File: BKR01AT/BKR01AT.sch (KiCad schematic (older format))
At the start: 44 parts, among them J1 Conn_02x03_Odd_Even, SW1 SW_Push, SW2 SW_Push, SW3 SW_Push, U1 LIS2DHTR, Y1 32MHz, Y2 32.768kHz

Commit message: WIP: PCB
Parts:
- AE1: footprint antena_ble:2450AT18B100 -> 2450AT18B100E:ANT_2450AT18B100E
- D1, D2, D3: footprint (none) -> LED_SMD:LED_0603_1608Metric
- FID1, FID2: footprint (none) -> Fiducial:Fiducial_0.5mm_Mask1mm
- MCU1: footprint (none) -> Package_DFN_QFN:QFN-48-1EP_6x6mm_P0.4mm_EP4.6x4.6mm
- SW1, SW2, SW3: footprint (none) -> Button_Switch_THT:SW_PUSH_6mm_H4.3mm
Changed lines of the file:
@@
 F 0 "SW1" H 9650 5530 50  0000 C CNN
 F 1 "SW_Push" H 9650 5439 50  0000 C CNN
-F 2 "" H 9650 5445 50  0001 C CNN
+F 2 "Button_Switch_THT:SW_PUSH_6mm_H4.3mm" H 9650 5445 50  0001 C CNN
 F 3 "~" H 9650 5445 50  0001 C CNN
 F 4 "PTS636 SL43 LFS" H 9650 5245 50  0001 C CNN "Part Number"
@@
 F 0 "SW3" H 8880 5550 50  0000 C CNN
 F 1 "SW_Push" H 8880 5459 50  0000 C CNN
-F 2 "" H 8880 5465 50  0001 C CNN
+F 2 "Button_Switch_THT:SW_PUSH_6mm_H4.3mm" H 8880 5465 50  0001 C CNN
 F 3 "~" H 8880 5465 50  0001 C CNN
 F 4 "PTS636 SL43 LFS" H 8880 5265 50  0001 C CNN "Part Number"
@@
 F 0 "SW2" H 8055 5535 50  0000 C CNN
 F 1 "SW_Push" H 8055 5444 50  0000 C CNN
-F 2 "" H 8055 5450 50  0001 C CNN
+F 2 "Button_Switch_THT:SW_PUSH_6mm_H4.3mm" H 8055 5450 50  0001 C CNN
 F 3 "~" H 8055 5450 50  0001 C CNN
 F 4 "PTS636 SL43 LFS" H 8055 5250 50  0001 C CNN "Part Number"
@@
 F 0 "D2" V 8752 3313 50  0000 L CNN
 F 1 "Red LED" V 8843 3313 50  0000 L CNN
-F 2 "" H 8805 3235 50  0001 C CNN
+F 2 "LED_SMD:LED_0603_1608Metric" H 8805 3235 50  0001 C CNN
 F 3 "~" H 8805 3235 50  0001 C CNN
 F 4 "150060VS75000" H 8805 3235 50  0001 C CNN "Part Number"
@@
 F 0 "D3" V 8012 3338 50  0000 L CNN
 F 1 "Red LED" V 8103 3338 50  0000 L CNN
-F 2 "" H 8065 3260 50  0001 C CNN
+F 2 "LED_SMD:LED_0603_1608Metric" H 8065 3260 50  0001 C CNN
 F 3 "~" H 8065 3260 50  0001 C CNN
 F 4 "150060RS75000" H 8065 3260 50  0001 C CNN "Part Number"
@@
 F 0 "D1" V 9562 3298 50  0000 L CNN
 F 1 "Green LED" V 9653 3298 50  0000 L CNN
-F 2 "" H 9615 3220 50  0001 C CNN
+F 2 "LED_SMD:LED_0603_1608Metric" H 9615 3220 50  0001 C CNN
 F 3 "~" H 9615 3220 50  0001 C CNN
 F 4 "150060VS75000" H 9615 3220 50  0001 C CNN "Part Number"
@@
 F 0 "FID2" H 7430 6176 50  0000 L CNN
 F 1 "Fiducial" H 7430 6085 50  0000 L CNN
-F 2 "" H 7345 6130 50  0001 C CNN
+F 2 "Fiducial:Fiducial_0.5mm_Mask1mm" H 7345 6130 50  0001 C CNN
 F 3 "~" H 7345 6130 50  0001 C CNN
 	1    7345 6130
@@
 F 0 "FID1" H 8095 6151 50  0000 L CNN
 F 1 "Fiducial" H 8095 6060 50  0000 L CNN
-F 2 "" H 8010 6105 50  0001 C CNN
+F 2 "Fiducial:Fiducial_0.5mm_Mask1mm" H 8010 6105 50  0001 C CNN
 F 3 "~" H 8010 6105 50  0001 C CNN
 	1    8010 6105
@@
 F 0 "MCU1" H 3600 3390 50  0000 L CNN
 F 1 "nRF52832-QFAB-R" H 3335 3305 50  0000 L CNN
-F 2 "" H 3705 3330 50  0001 C CNN
+F 2 "Package_DFN_QFN:QFN-48-1EP_6x6mm_P0.4mm_EP4.6x4.6mm" H 3705 3330 50  0001 C CNN
 F 3 "" H 3705 3330 50  0001 C CNN
 F 4 "nRF52832-QFAB-R" H 3705 3330 50  0001 C CNN "Part Number"
@@
 F 0 "AE1" H 2425 5684 50  0000 L CNN
 F 1 "Antenna" H 2425 5593 50  0000 L CNN
-F 2 "antena_ble:2450AT18B100" H 2345 5695 50  0001 C CNN
+F 2 "2450AT18B100E:ANT_2450AT18B100E" H 2345 5695 50  0001 C CNN
 F 3 "~" H 2345 5695 50  0001 C CNN
 F 4 "2450AT18B100E" H 2345 5695 50  0001 C CNN "Part Number"
@@
 	3005 6510 3005 7645
 $Comp
-L power:VDD #PWR?
+L power:VDD #PWR0101
 U 1 1 5E5987B3
 P 8065 2790
-F 0 "#PWR?" H 8065 2640 50  0001 C CNN
+F 0 "#PWR0101" H 8065 2640 50  0001 C CNN
 F 1 "VDD" H 8082 2963 50  0000 C CNN
 F 2 "" H 8065 2790 50  0001 C CNN
@@
 $EndComp
 $Comp
-L power:VDD #PWR?
+L power:VDD #PWR0102
 U 1 1 5E59EF9F
 P 8805 2765
-F 0 "#PWR?" H 8805 2615 50  0001 C CNN
+F 0 "#PWR0102" H 8805 2615 50  0001 C CNN
 F 1 "VDD" H 8822 2938 50  0000 C CNN
 F 2 "" H 8805 2765 50  0001 C CNN
@@
 $EndComp
 $Comp
-L power:VDD #PWR?
+L power:VDD #PWR0103
 U 1 1 5E5A4F33
 P 9615 2750
-F 0 "#PWR?" H 9615 2600 50  0001 C CNN
+F 0 "#PWR0103" H 9615 2600 50  0001 C CNN
 F 1 "VDD" H 9632 2923 50  0000 C CNN
 F 2 "" H 9615 2750 50  0001 C CNN
@@
 	8055 4745 8055 4690
 $Comp
-L power:VDD #PWR?
+L power:VDD #PWR0104
 U 1 1 5E5B249E
 P 8055 4690
-F 0 "#PWR?" H 8055 4540 50  0001 C CNN
+F 0 "#PWR0104" H 8055 4540 50  0001 C CNN
 F 1 "VDD" H 8072 4863 50  0000 C CNN
 F 2 "" H 8055 4690 50  0001 C CNN
@@
 $EndComp
 $Comp
-L power:VDD #PWR?
+L power:VDD #PWR0105
 U 1 1 5E5B8527
 P 8880 4705
-F 0 "#PWR?" H 8880 4555 50  0001 C CNN
+F 0 "#PWR0105" H 8880 4555 50  0001 C CNN
 F 1 "VDD" H 8897 4878 50  0000 C CNN
 F 2 "" H 8880 4705 50  0001 C CNN
@@
 $EndComp
 $Comp
-L power:VDD #PWR?
+L power:VDD #PWR0106
 U 1 1 5E5BE646
 P 9650 4685
-F 0 "#PWR?" H 9650 4535 50  0001 C CNN
+F 0 "#PWR0106" H 9650 4535 50  0001 C CNN
 F 1 "VDD" H 9667 4858 50  0000 C CNN
 F 2 "" H 9650 4685 50  0001 C CNN

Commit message: PCB: trilhas
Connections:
- net ac_INT1: now also MCU1.38 (P0.26); no longer MCU1.37 (P0.25)
- net ac_INT2: now also MCU1.37 (P0.25); no longer MCU1.38 (P0.26)
- net b_F1: now also MCU1.18 (P.015); no longer MCU1.17 (P.014)
- net b_F2: now also MCU1.19 (P.016); no longer MCU1.18 (P.015)
- net b_RST: now also MCU1.17 (P.014); no longer MCU1.19 (P.016)
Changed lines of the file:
@@
 Wire Wire Line
 	8055 5040 8055 5050
+Text GLabel 3555 4535 3    50   Input ~ 0
+b_RST
+Text GLabel 3655 4535 3    50   Input ~ 0
+b_F1
 Text GLabel 3755 4535 3    50   Input ~ 0
-b_RST
-Text GLabel 3555 4535 3    50   Input ~ 0
-b_F1
-Text GLabel 3655 4535 3    50   Input ~ 0
 b_F2
 Wire Wire Line
@@
 Wire Wire Line
 	1130 7275 1435 7275
-Text GLabel 4880 3680 2    50   Input ~ 0
-tag_RST
 Text GLabel 4875 3780 2    50   Input ~ 0
 tag_SWDIO
@@
 Text GLabel 3955 2225 1    50   Input ~ 0
 ac_SDO_SAO
+Text GLabel 4255 2225 1    50   Input ~ 0
+ac_INT2
 Text GLabel 4155 2225 1    50   Input ~ 0
-ac_INT2
-Text GLabel 4255 2225 1    50   Input ~ 0
 ac_INT1
 Text GLabel 3855 2225 1    50   Input ~ 0
@@
 NoConn ~ 4055 4380
 NoConn ~ 4155 4380
-NoConn ~ 4255 4380
-Wire Wire Line
-	4880 3680 4755 3680
 $Comp
 L Device:C_Small C13
@@
 $EndComp
 NoConn ~ 5045 6905
+Wire Wire Line
+	4880 3680 4755 3680
+Text GLabel 4880 3680 2    50   Input ~ 0
+tag_RST
+NoConn ~ 4255 4380
 $EndSCHEMATC

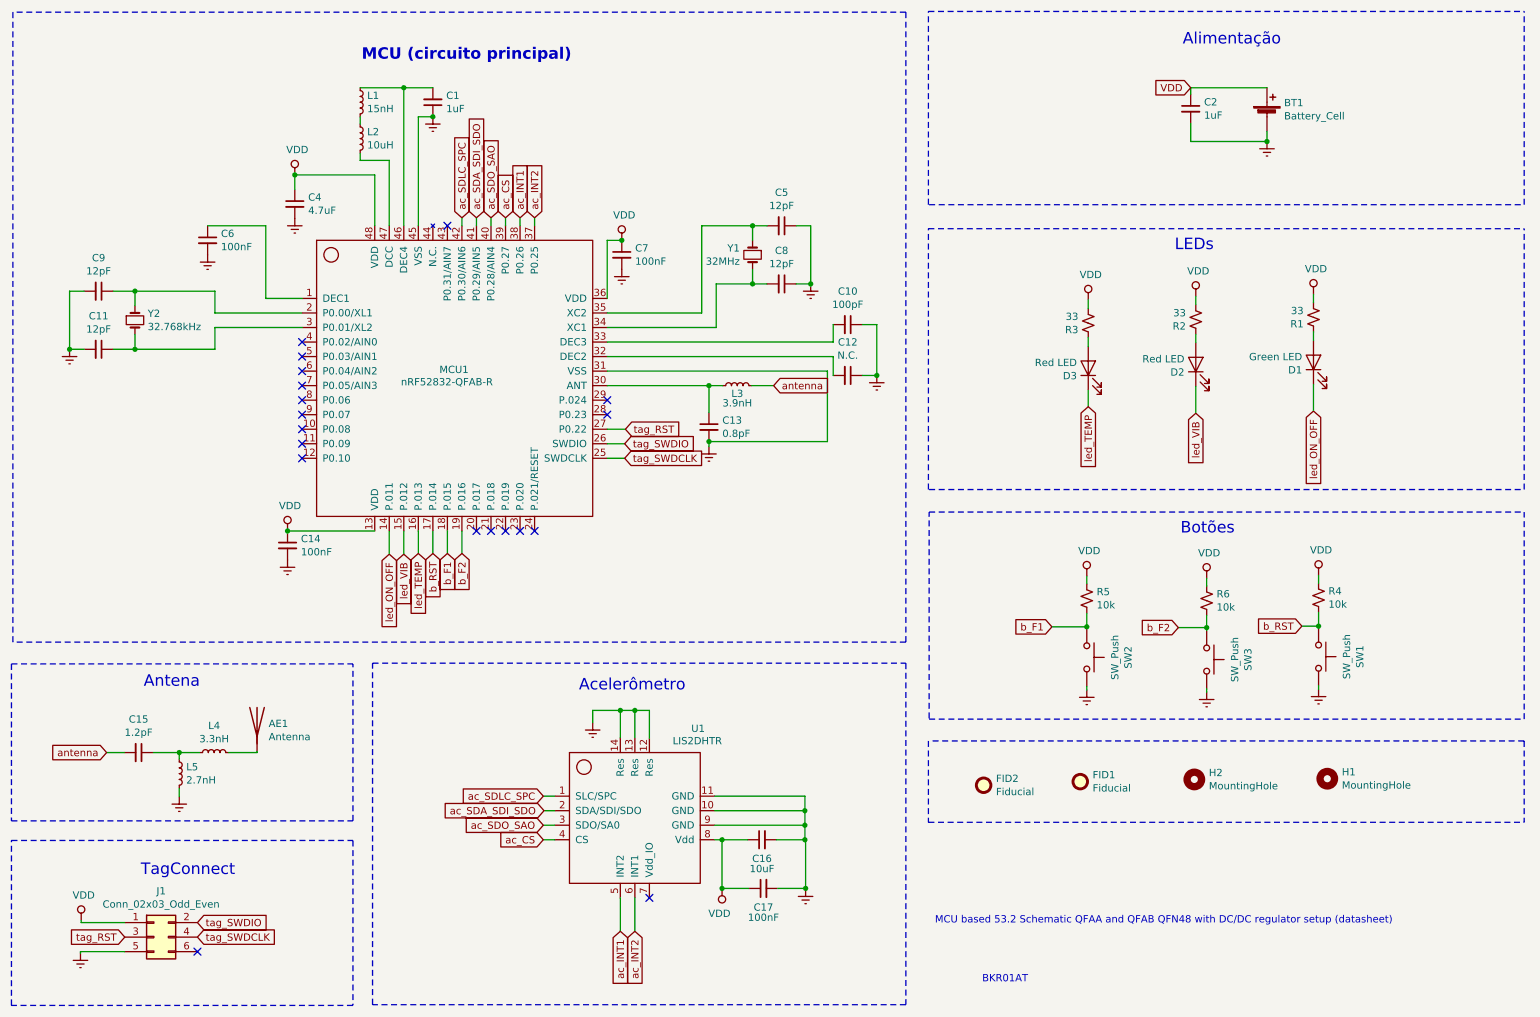
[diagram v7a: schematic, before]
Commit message: PCB
trilhas de alimentação, shielding e stitching da antena
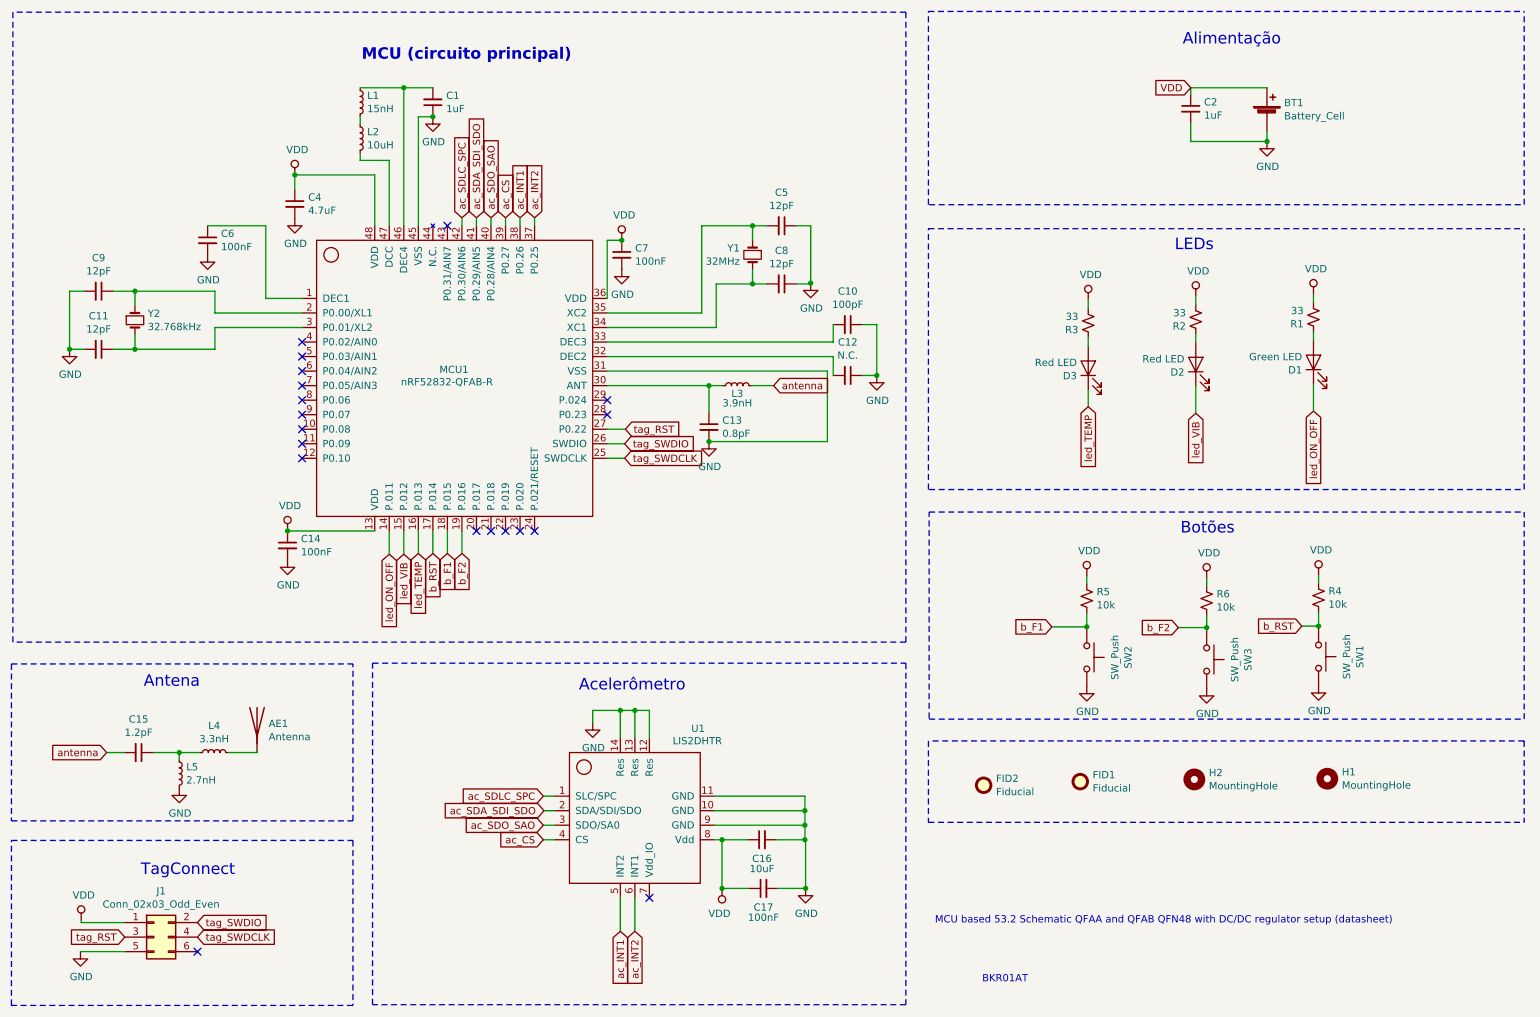
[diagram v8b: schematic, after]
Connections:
- net Earth renamed GND
